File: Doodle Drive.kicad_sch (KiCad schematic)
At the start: 32 parts, among them J1 USB_B, J2 PINHD_1x4_Male, J6 PINHD_1x2_Male, SW1 Push_Button, SW2 Push_Button, SW3 Push_Button, U1 STM32F411RETx, U6 AP7343-30W5-7, Y1 32.768KHz ±20ppm 12.5pF, Y2 25MHZ 9PF

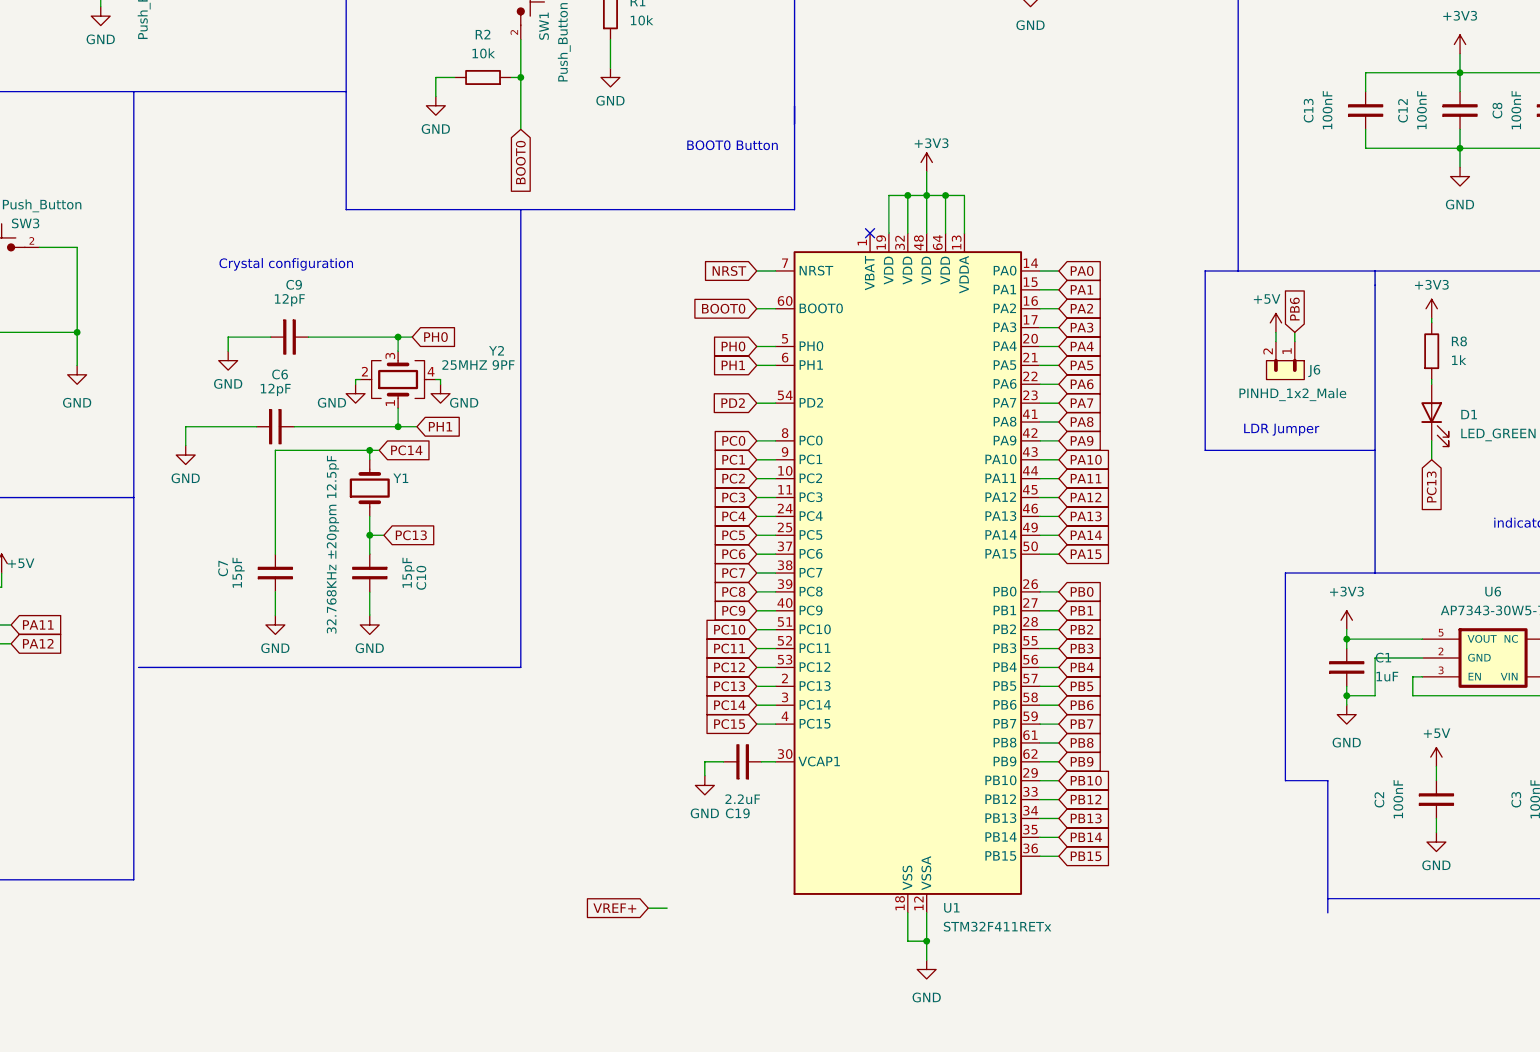
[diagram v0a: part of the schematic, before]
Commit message: cleaned up main schematic
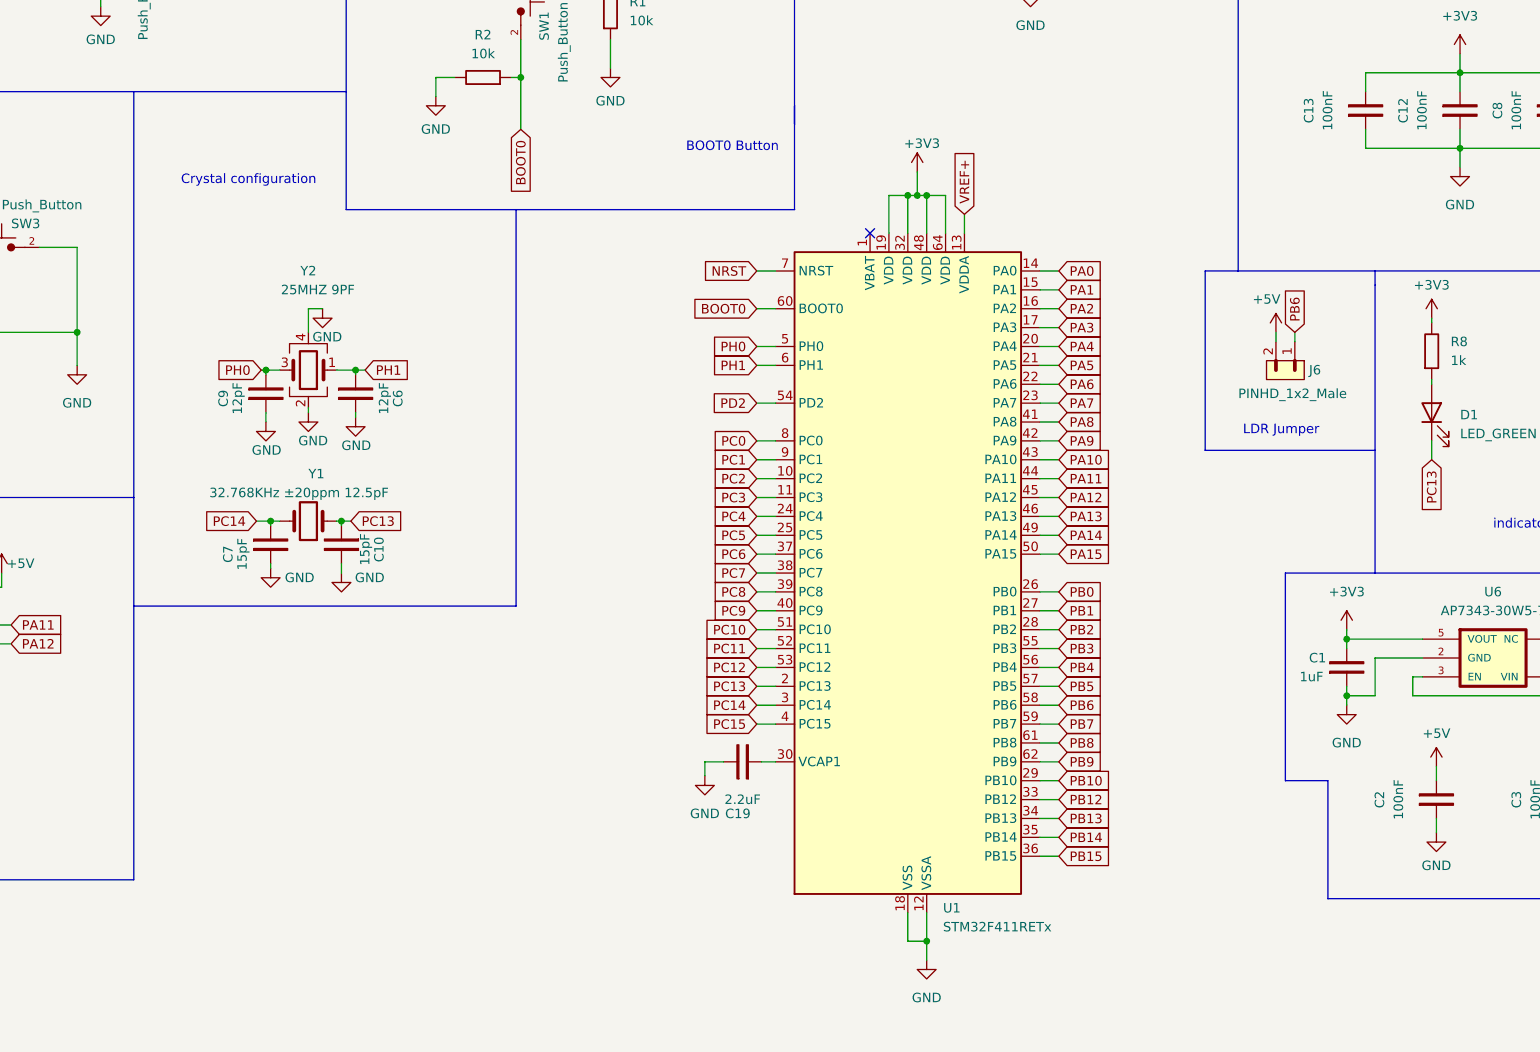
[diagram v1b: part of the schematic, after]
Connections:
- net +3V3: no longer U1.13 (VDDA)
- net VREF+: now also U1.13 (VDDA)
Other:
- moved on the sheet: C10, C6, C9, Y1, Y2

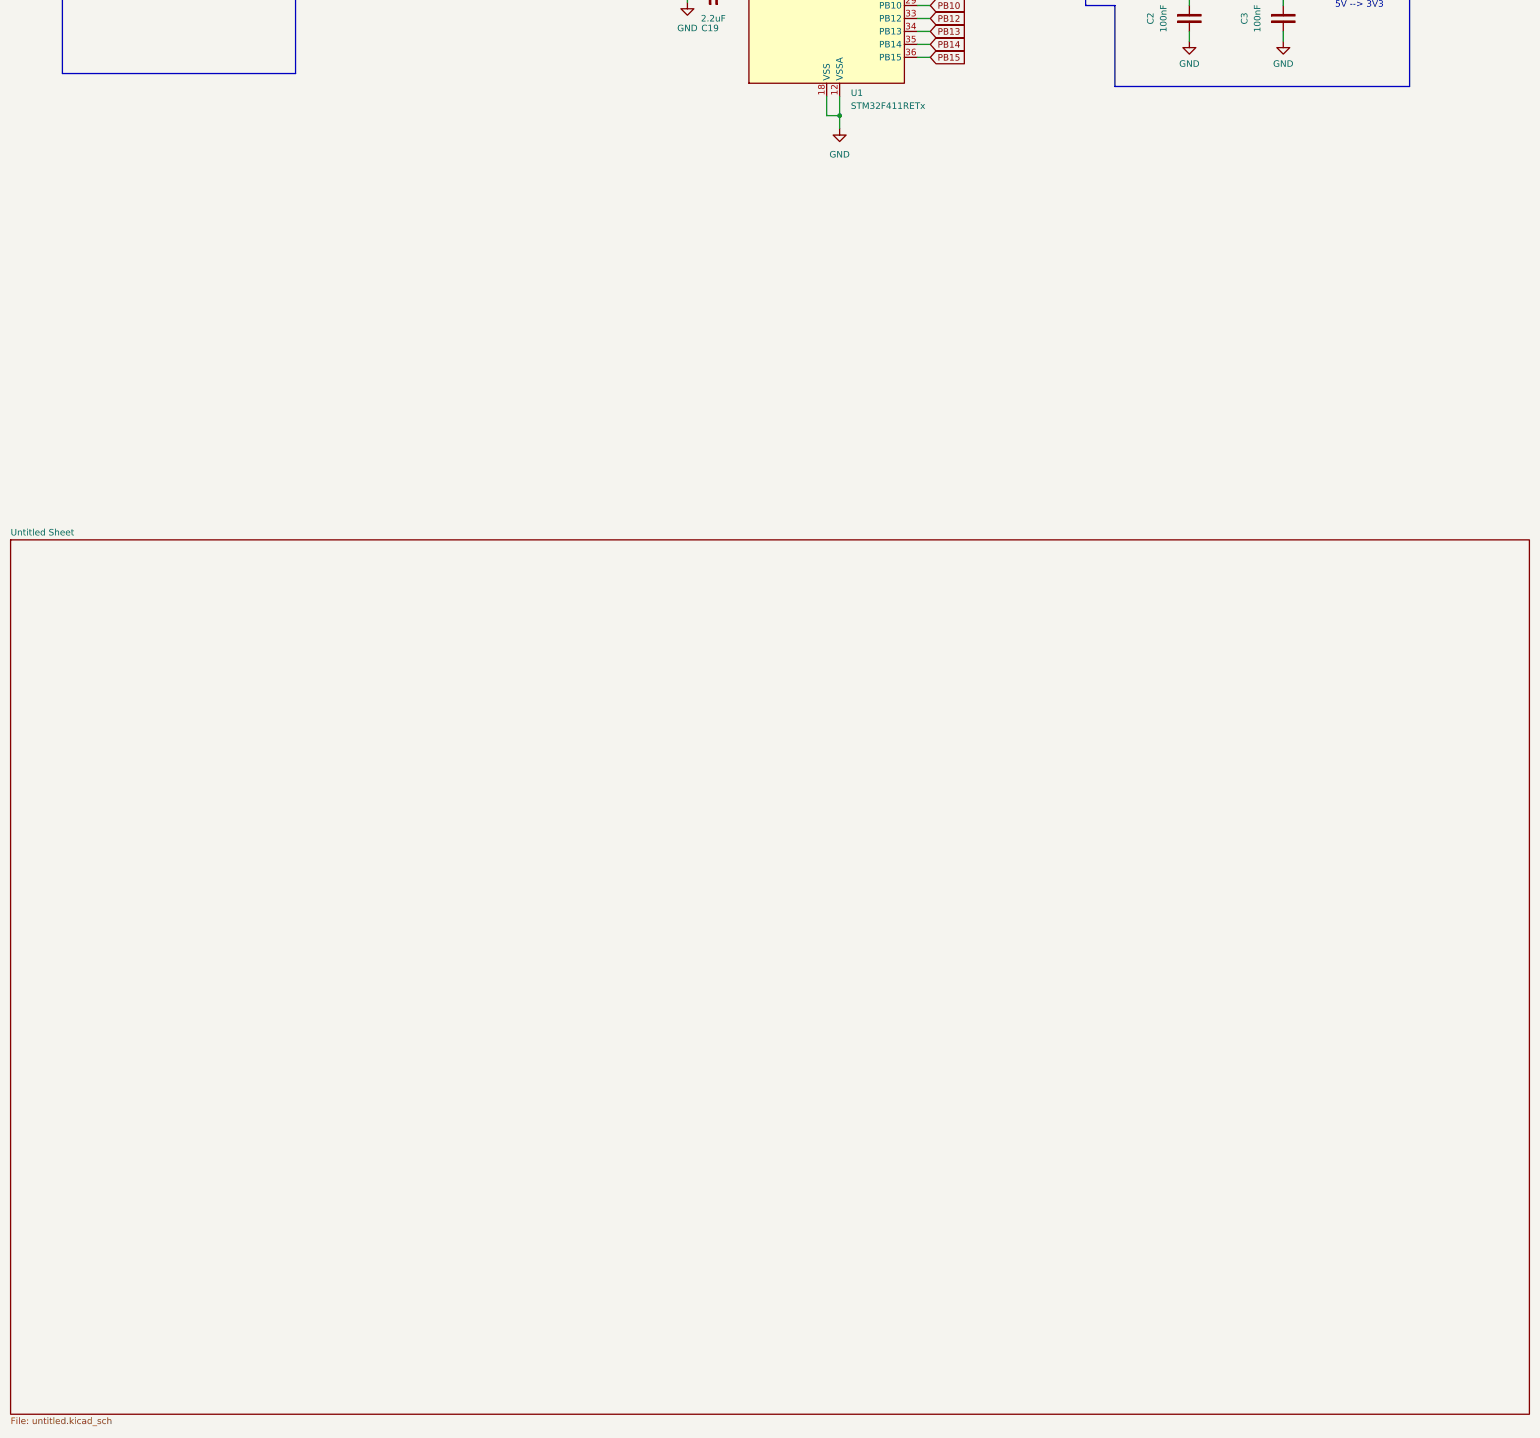
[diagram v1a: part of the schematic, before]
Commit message: Divide DRV8825s in two sheets, and connect their pins to stm32
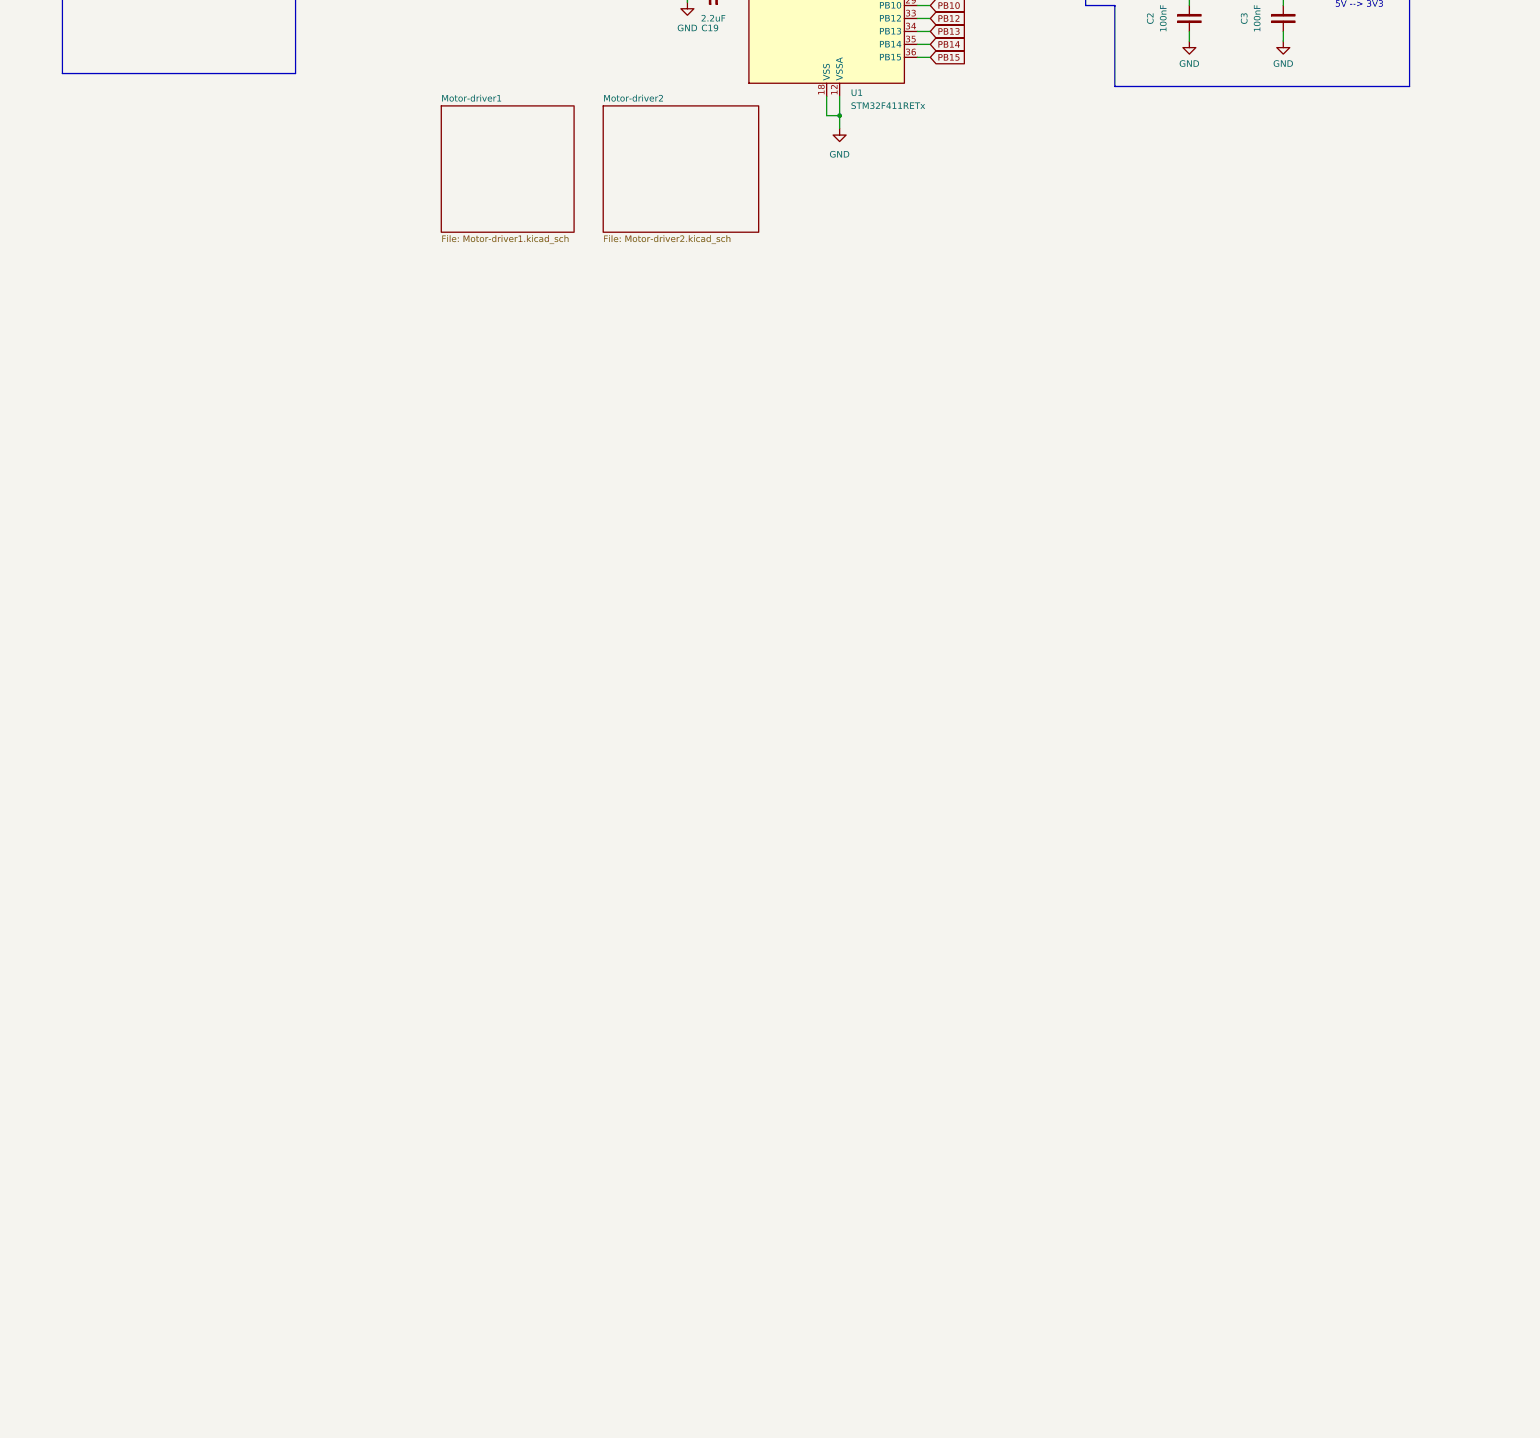
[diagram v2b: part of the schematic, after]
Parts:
- C1: footprint Capacitor_SMD:C_0805_2012Metric -> (none)
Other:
- removed sheet Untitled Sheet
- added sheet Motor-driver1 (Motor-driver1.kicad_sch)
- added sheet Motor-driver2 (Motor-driver2.kicad_sch)
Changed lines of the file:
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@@
       (effects (font (size 1.27 1.27)) (justify right))
     )
-    (property "Footprint" "Capacitor_SMD:C_0805_2012Metric" (at 231.14 130.81 0)
+    (property "Footprint" "" (at 231.14 130.81 0)
       (effects (font (size 1.27 1.27)) hide)
     )
@@
     )
   )
-  (sheet (at 8.255 250.825) (size 297.815 171.45) (fields_autoplaced)
+  (sheet (at 124.46 165.735) (size 30.48 24.765) (fields_autoplaced)
     (stroke (width 0.1524) (type solid))
     (fill (color 0 0 0 0.0000))
-    (property "Sheetname" "Untitled Sheet" (at 8.255 250.1134 0)
+    (property "Sheetname" "Motor-driver2" (at 124.46 165.0234 0)
       (effects (font (size 1.27 1.27)) (justify left bottom))
     )
-    (property "Sheetfile" "untitled.kicad_sch" (at 8.255 422.8596 0)
+    (property "Sheetfile" "Motor-driver2.kicad_sch" (at 124.46 191.0846 0)
       (effects (font (size 1.27 1.27)) (justify left top))
     )
     (instances
       (project "Doodle Drive"
-        (path "/3ec634aa-8c09-482d-9325-2288a4dbd68b" (page "2"))
-      )
-    )
+        (path "/3ec634aa-8c09-482d-9325-2288a4dbd68b" (page "3"))
+      )
+    )
+  )
+  (sheet (at 92.71 165.735) (size 26.035 24.765) (fields_autoplaced)
+    (stroke (width 0.1524) (type solid))
+    (fill (color 0 0 0 0.0000))
+    (property "Sheetname" "Motor-driver1" (at 92.71 165.0234 0)
+      (effects (font (size 1.27 1.27)) (justify left bottom))
+    )
+    (property "Sheetfile" "Motor-driver1.kicad_sch" (at 92.71 191.0846 0)
+      (effects (font (size 1.27 1.27)) (justify left top))
+    )
+    (instances
+      (project "Doodle Drive"
+        (path "/3ec634aa-8c09-482d-9325-2288a4dbd68b" (page "4"))
+      )
+    )
